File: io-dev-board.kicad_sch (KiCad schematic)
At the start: 67 parts, among them IC1 24LC01B_P, J1 PWR, J2 SW_Conn, J3 LED_Conn, J4 I2C_Conn, J5 Rot_Conn, Q1 Q_NPN, Q2 Q_NPN, Q3 Q_NPN, Q4 Q_NPN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

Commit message: add '3.3V!' label to board, remove floating 'not connected' mark
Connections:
- no-connect marks 6 -> 5
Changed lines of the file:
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@@
 		(at 81.28 175.26)
-	)
-	(no_connect
-		(at 394.97 2.54)
 	)
 	(wire

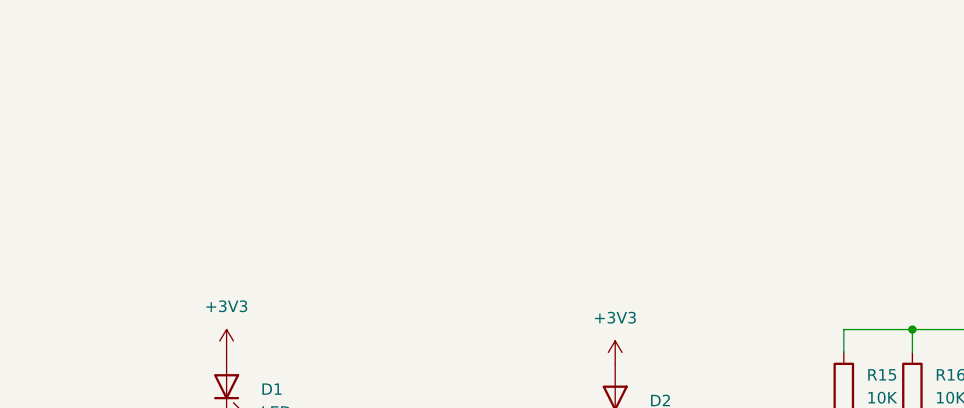
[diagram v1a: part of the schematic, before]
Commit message: refactor: add LED and NPN resistor calculation hints
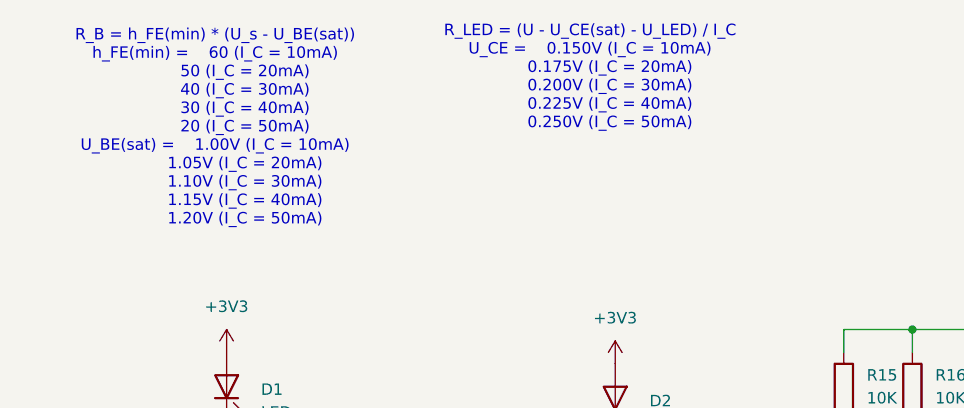
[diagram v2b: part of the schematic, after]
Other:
- note added: "R_B = h_FE(min) * (U_s - U_BE(sat)) h_FE(min) = 60 (I_C = 10mA) 50 (I_C = 20mA) 40 (I_C = 30mA) 30 (I_C = 40mA) 20 (I_C = 50mA) U_BE(sat) = 1.00V (I_C = 10mA) 1.05V (I_C = 20mA) 1.10V (I_C = 30mA) 1.15V (I_C = 40mA) 1.20V (I_C = 50mA)"
- note added: "R_LED = (U - U_CE(sat) - U_LED) / I_C U_CE = 0.150V (I_C = 10mA) 0.175V (I_C = 20mA) 0.200V (I_C = 30mA) 0.225V (I_C = 40mA) 0.250V (I_C = 50mA)"
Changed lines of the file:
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@@
 	(generator_version "10.0")
 	(paper "A4")
+	(text "R_LED = (U - U_CE(sat) - U_LED) / I_C\nU_CE =	0.150V (I_C = 10mA)\n		0.175V (I_C = 20mA)\n		0.200V (I_C = 30mA)\n		0.225V (I_C = 40mA)\n		0.250V (I_C = 50mA)"
+		(exclude_from_sim no)
+		(at 77.216 -7.62 0)
+		(effects
+			(font
+				(size 1.27 1.27)
+			)
+		)
+	)
+	(text "R_B = h_FE(min) * (U_s - U_BE(sat))\nh_FE(min) =	60 (I_C = 10mA)\n			50 (I_C = 20mA)\n			40 (I_C = 30mA)\n			30 (I_C = 40mA)\n			20 (I_C = 50mA)\nU_BE(sat) =	1.00V (I_C = 10mA)\n			1.05V (I_C = 20mA)\n			1.10V (I_C = 30mA)\n			1.15V (I_C = 40mA)\n			1.20V (I_C = 50mA)"
+		(exclude_from_sim no)
+		(at 35.56 -2.032 0)
+		(effects
+			(font
+				(size 1.27 1.27)
+			)
+		)
+	)
 	(junction
 		(at 152.4 134.62)

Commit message: fix: add missing 'I_C' to resistor calculation
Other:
- note added: "R_B = h_FE(min) * (U_s - U_BE(sat)) / I_C h_FE(min) = 60 (I_C = 10mA) 50 (I_C = 20mA) 40 (I_C = 30mA) 30 (I_C = 40mA) 20 (I_C = 50mA) U_BE(sat) = 1.00V (I_C = 10mA) 1.05V (I_C = 20mA) 1.10V (I_C = 30mA) 1.15V (I_C = 40mA) 1.20V (I_C = 50mA)"
- note removed: "R_B = h_FE(min) * (U_s - U_BE(sat)) h_FE(min) = 60 (I_C = 10mA) 50 (I_C = 20mA) 40 (I_C = 30mA) 30 (I_C = 40mA) 20 (I_C = 50mA) U_BE(sat) = 1.00V (I_C = 10mA) 1.05V (I_C = 20mA) 1.10V (I_C = 30mA) 1.15V (I_C = 40mA) 1.20V (I_C = 50mA)"
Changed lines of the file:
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@@
 		)
 	)
-	(text "R_B = h_FE(min) * (U_s - U_BE(sat))\nh_FE(min) =	60 (I_C = 10mA)\n			50 (I_C = 20mA)\n			40 (I_C = 30mA)\n			30 (I_C = 40mA)\n			20 (I_C = 50mA)\nU_BE(sat) =	1.00V (I_C = 10mA)\n			1.05V (I_C = 20mA)\n			1.10V (I_C = 30mA)\n			1.15V (I_C = 40mA)\n			1.20V (I_C = 50mA)"
+	(text "R_B = h_FE(min) * (U_s - U_BE(sat)) / I_C\nh_FE(min) =	60 (I_C = 10mA)\n			50 (I_C = 20mA)\n			40 (I_C = 30mA)\n			30 (I_C = 40mA)\n			20 (I_C = 50mA)\nU_BE(sat) =	1.00V (I_C = 10mA)\n			1.05V (I_C = 20mA)\n			1.10V (I_C = 30mA)\n			1.15V (I_C = 40mA)\n			1.20V (I_C = 50mA)"
 		(exclude_from_sim no)
-		(at 35.56 -2.032 0)
+		(at 32.004 -2.794 0)
 		(effects
 			(font
